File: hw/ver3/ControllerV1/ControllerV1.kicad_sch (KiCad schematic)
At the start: 96 parts, among them J1 SWD Debug, J2 BMS_Serial, J3 Debug, P1 USB_C_Plug_USB2.0, Q1 BSS138, Q2 BSS138, Q3 BSS138, Q4 BSS138, SW1 Boot, SW2 Reset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

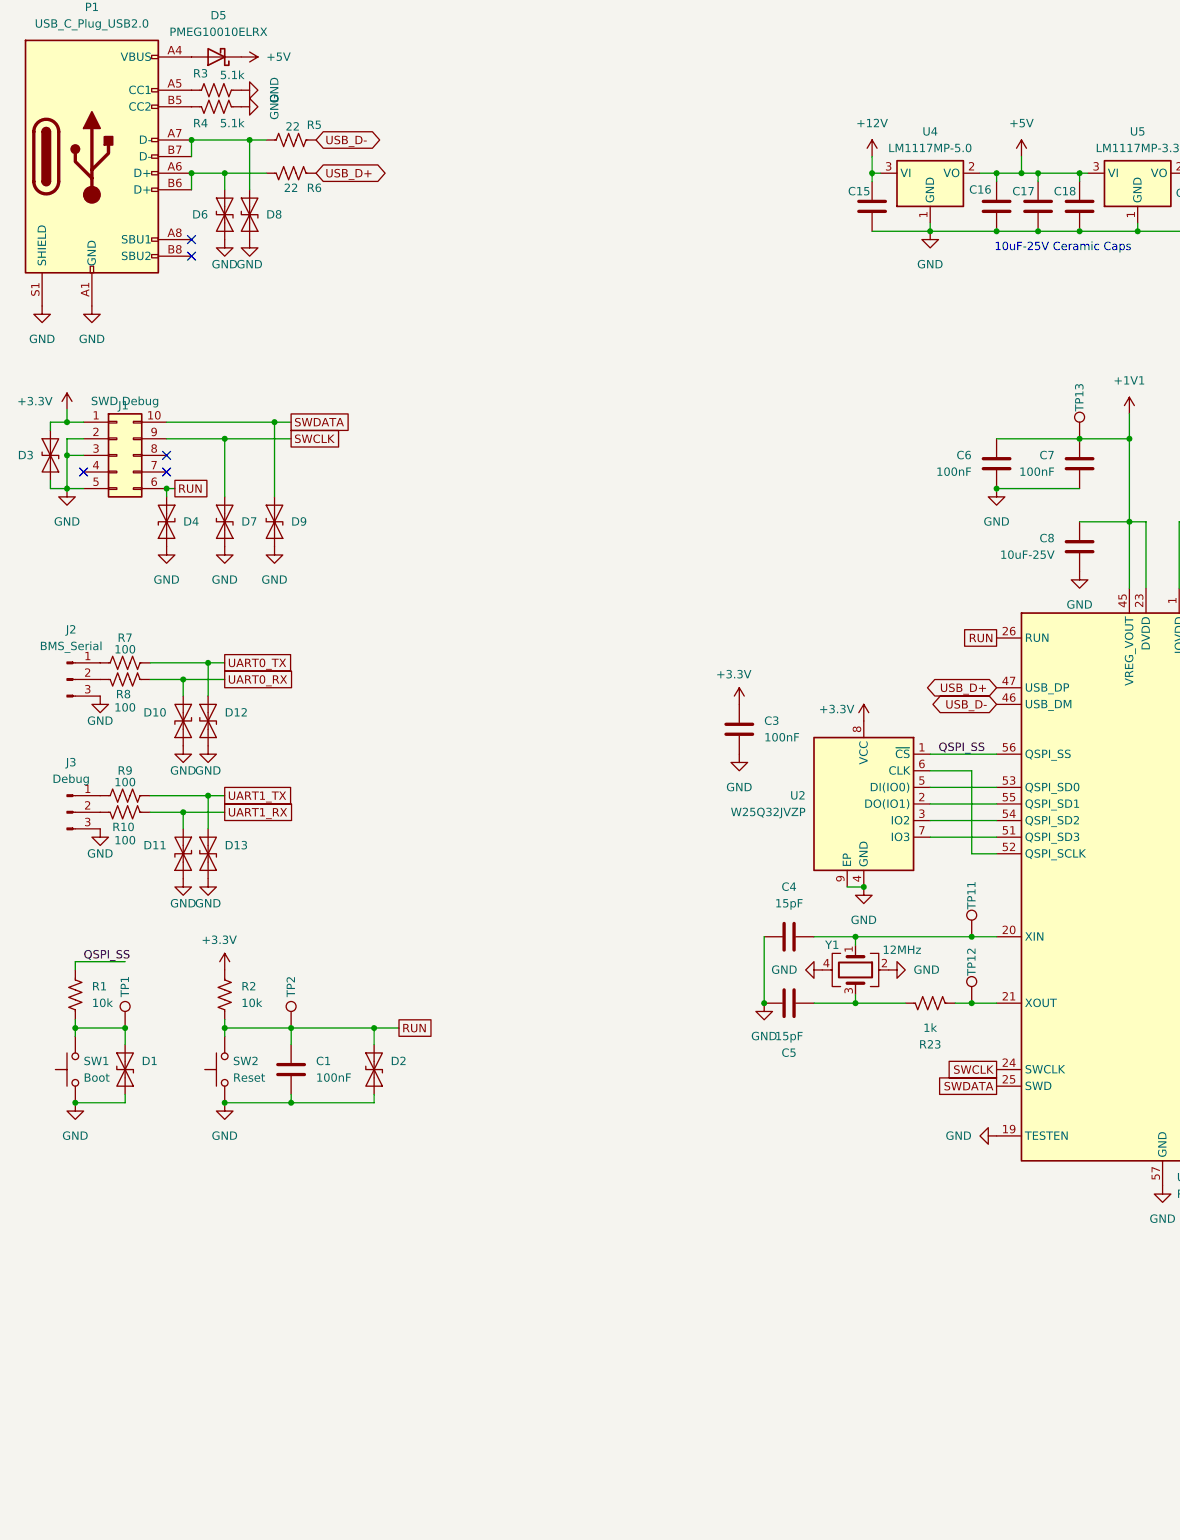
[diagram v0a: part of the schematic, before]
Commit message: Split the design into four major components. Start working on system architecture.
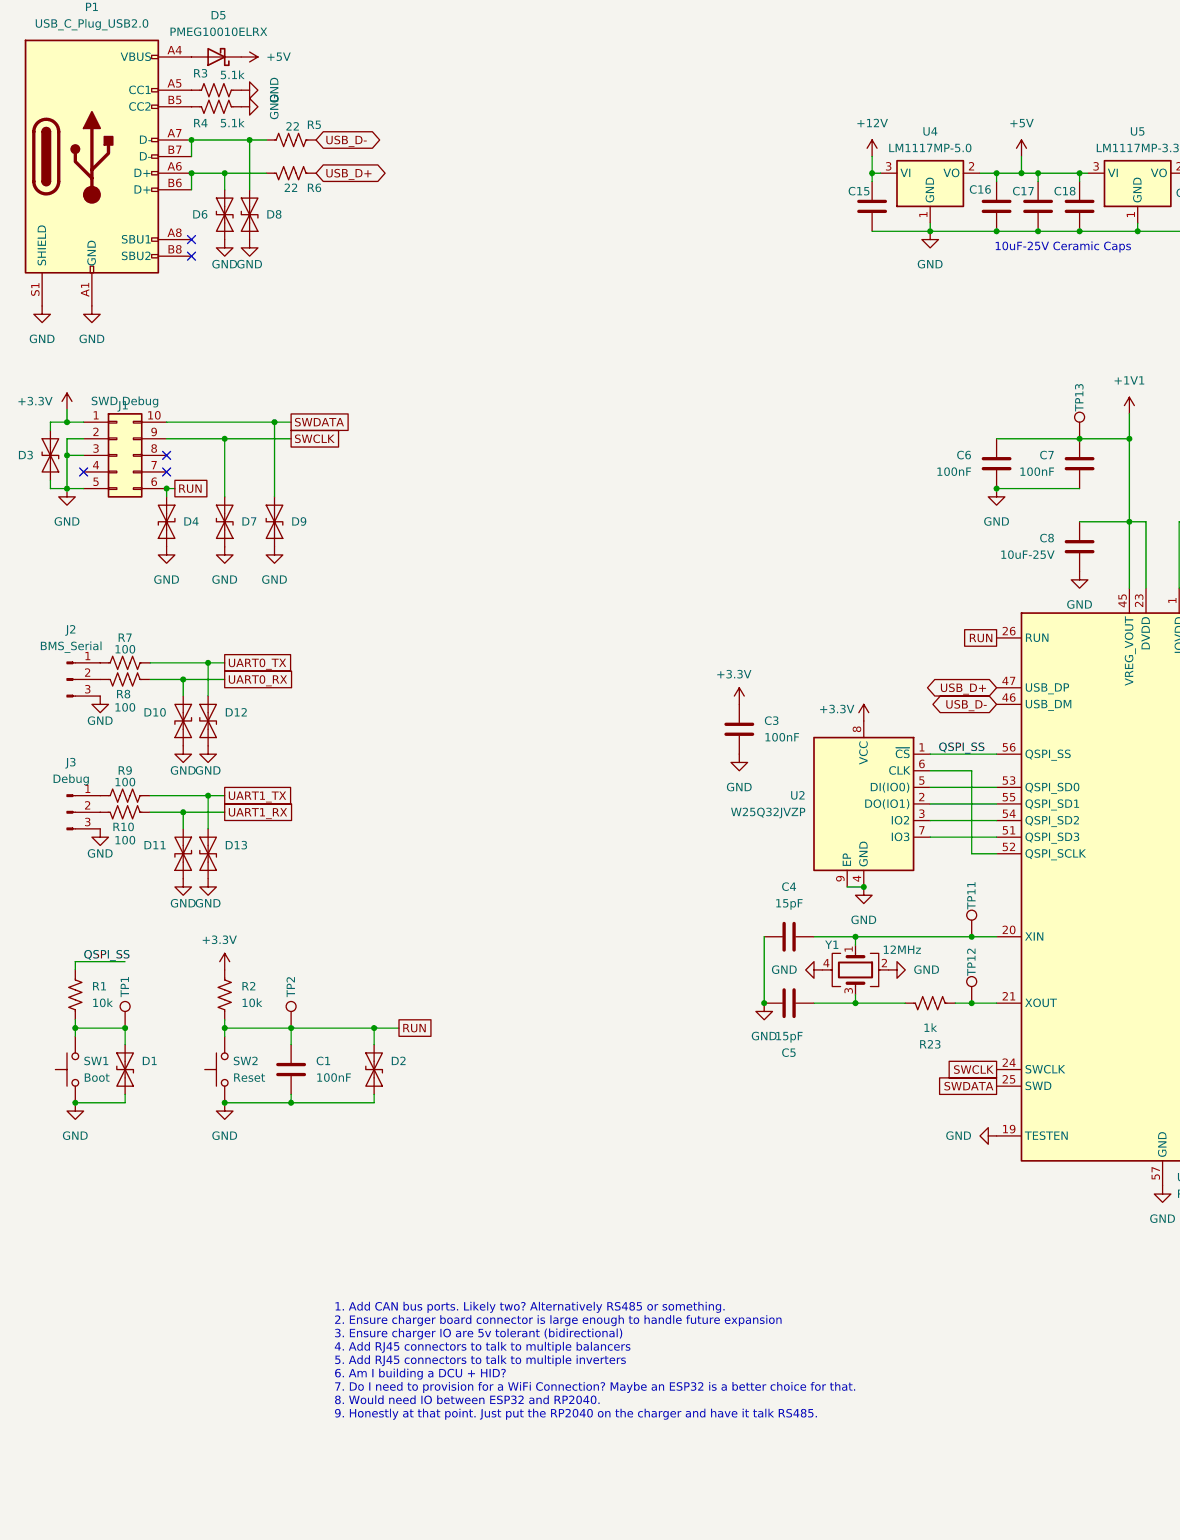
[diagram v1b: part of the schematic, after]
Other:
- note added: "1. Add CAN bus ports. Likely two? Alternatively RS485 or something. 2. Ensure charger board connector is large enough to handle future expansion 3. Ensure charger IO are 5v tolerant (bidirectional) 4. Add RJ45 connectors to talk to multiple balancers 5. Add RJ45 connectors to talk to multiple inverters 6. Am I building a DCU + HID? 7. Do I need to provision for a WiFi Connection? Maybe an ESP32 i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"
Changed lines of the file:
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@@
 (kicad_sch
-	(version 20231120)
+	(version 20250114)
 	(generator "eeschema")
-	(generator_version "8.0")
+	(generator_version "9.0")
 	(paper "A3")
+	(text "10uF-25V Ceramic Caps"
+		(exclude_from_sim no)
+		(at 177.8 53.34 0)
+		(effects
+			(font
+				(size 1.27 1.27)
+			)
+		)
+	)
+	(text "1. Add CAN bus ports. Likely two? Alternatively RS485 or something.\n2. Ensure charger board connector is large enough to handle future expansion\n3. Ensure charger IO are 5v tolerant (bidirectional)\n4. Add RJ45 connectors to talk to multiple balancers\n5. Add RJ45 connectors to talk to multiple inverters\n6. Am I building a DCU + HID?\n7. Do I need to provision for a WiFi Connection? Maybe an ESP32 is a better choice for that.\n8. Would need IO between ESP32 and RP2040.\n9. Honestly at that point. Just put the RP2040 on the charger and have it talk RS485."
+		(exclude_from_sim no)
+		(at 66.294 223.774 0)
+		(effects
+			(font
+				(size 1.27 1.27)
+			)
+			(justify left)
+		)
+	)
 	(junction
 		(at 369.57 54.61)
@@
 		)
 	)
-	(text "10uF-25V Ceramic Caps"
-		(exclude_from_sim no)
-		(at 177.8 53.34 0)
-		(effects
-			(font
-				(size 1.27 1.27)
-			)
-		)
-	)
 	(label "QSPI_SS"
 		(at 27.94 162.56 0)
-		(fields_autoplaced yes)
 		(effects
 			(font
@@
 	(label "SPI1_SCK"
 		(at 219.71 148.59 0)
-		(fields_autoplaced yes)
 		(effects
 			(font
@@
 	(label "SPI1_CSn"
 		(at 361.95 165.1 0)
-		(fields_autoplaced yes)
 		(effects
 			(font
@@
 	(label "SPI1_RX"
 		(at 219.71 143.51 0)
-		(fields_autoplaced yes)
 		(effects
 			(font
@@
 	(label "SPI0_RX"
 		(at 359.41 184.15 0)
-		(fields_autoplaced yes)
 		(effects
 			(font
@@
 	(label "SPI0_RX"
 		(at 219.71 113.03 0)
-		(fields_autoplaced yes)
 		(effects
 			(font
@@
 	(label "QSPI_SS"
 		(at 158.75 130.81 0)
-		(fields_autoplaced yes)
 		(effects
 			(font
@@
 	(label "SPI1_RX"
 		(at 361.95 162.56 0)
-		(fields_autoplaced yes)
 		(effects
 			(font
@@
 	(label "SPI0_SCK"
 		(at 219.71 118.11 0)
-		(fields_autoplaced yes)
 		(effects
 			(font
@@
 	(label "SPI0_CSn"
 		(at 219.71 115.57 0)
-		(fields_autoplaced yes)
 		(effects
 			(font
@@
 	(label "SPI1_TX"
 		(at 219.71 151.13 0)
-		(fields_autoplaced yes)
 		(effects
 			(font
@@
 	(label "SPI0_TX"
 		(at 359.41 181.61 0)
-		(fields_autoplaced yes)
 		(effects
 			(font
@@
 	(label "SPI1_CSn"
 		(at 219.71 146.05 0)
-		(fields_autoplaced yes)
 		(effects
 			(font
@@
 	(label "SPI1_SCK"
 		(at 361.95 167.64 0)
-		(fields_autoplaced yes)
 		(effects
 			(font
@@
 	(label "SPI0_CSn"
 		(at 359.41 176.53 0)
-		(fields_autoplaced yes)
 		(effects
 			(font
@@
 	(label "SPI1_TX"
 		(at 361.95 170.18 0)
-		(fields_autoplaced yes)
 		(effects
 			(font
@@
 	(label "SPI0_TX"
 		(at 219.71 120.65 0)
-		(fields_autoplaced yes)
 		(effects
 			(font
@@
 	(label "SPI0_SCK"
 		(at 359.41 179.07 0)
-		(fields_autoplaced yes)
 		(effects
 			(font
@@
 		(shape output)
 		(at 227.33 151.13 0)
-		(fields_autoplaced yes)
 		(effects
 			(font
@@
 		(shape output)
 		(at 218.44 140.97 0)
-		(fields_autoplaced yes)
 		(effects
 			(font
@@
 		(shape input)
 		(at 218.44 189.23 0)
-		(fields_autoplaced yes)
 		(effects
 			(font
@@
 		(shape output)
 		(at 227.33 148.59 0)
-		(fields_autoplaced yes)
 		(effects
 			(font
@@
 		(shape input)
 		(at 227.33 143.51 0)
-		(fields_autoplaced yes)
 		(effects
 			(font
@@
 		(shape output)
 		(at 227.33 146.05 0)
-		(fields_autoplaced yes)
 		(effects
 			(font
@@
 		)
 	)
+	(embedded_fonts no)
 )

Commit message: Redo some charger routing. Improve design for interconnect
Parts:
- removed C1, C11, C12, C13, C14, C2, C22, C3, C6, C7, C9: 100nF, Capacitor_SMD:C_0603_1608Metric, symbol Device:C
- removed C10, C15, C16, C17, C18, C19, C20, C21, C8: 10uF-25V, Capacitor_SMD:C_0603_1608Metric, symbol Device:C
- removed C4, C5: 15pF, Capacitor_SMD:C_0603_1608Metric, symbol Device:C
- removed D1, D10, D11, D12, D13, D18, D2: ESD9B3.3ST5G, Diode_SMD:D_SOD-923, symbol Diode:ESD9B3.3ST5G
- removed D14, D16: Yellow LED, LED_SMD:LED_0805_2012Metric, symbol Device:LED
- removed D15, D17: Green LED, LED_SMD:LED_0805_2012Metric, symbol Device:LED
- removed D3, D4, D6, D7, D8, D9: ESD9B5.0ST5G, Diode_SMD:D_SOD-923, symbol Diode:ESD9B5.0ST5G
- removed D5: PMEG10010ELRX, Diode_SMD:D_SOD-123, symbol Device:D_Schottky
- removed J1: SWD Debug, Connectors:JTAG_2x05_P1_27mm_Shrouded_SMD, symbol Connector_Generic:Conn_02x05_Counter_Clockwise
- removed J2: BMS_Serial, Connector_PinHeader_2.54mm:PinHeader_1x03_P2.54mm_Vertical, symbol Connector:Conn_01x03_Pin
- removed J3: Debug, Connector_PinHeader_2.54mm:PinHeader_1x03_P2.54mm_Vertical, symbol Connector:Conn_01x03_Pin
- removed P1: USB_C_Plug_USB2.0, Connector_USB:USB_C_Receptacle_GCT_USB4085, symbol Connector:USB_C_Receptacle_USB2.0_16P
- removed Q1, Q2, Q3, Q4: BSS138, Package_TO_SOT_SMD:SOT-23, symbol Transistor_FET:BSS138
- removed R1, R13, R14, R19, R2, R20, R25: 10k, Resistor_SMD:R_0603_1608Metric, symbol Device:R_US
- removed R10, R11, R12, R17, R18, R7, R8, R9: 100, Resistor_SMD:R_0603_1608Metric, symbol Device:R_US
- removed R15, R16, R21, R22: 510, Resistor_SMD:R_0603_1608Metric, symbol Device:R_US
- removed R23: 1k, Resistor_SMD:R_0603_1608Metric, symbol Device:R_US
- removed R24, R26: 100k, Resistor_SMD:R_0603_1608Metric, symbol Device:R_US
- removed R3, R4: 5.1k, Resistor_SMD:R_0603_1608Metric, symbol Device:R_US
- removed R5, R6: 22, Resistor_SMD:R_0603_1608Metric, symbol Device:R_US
- removed SW1: Boot, Button_Switch_SMD:SW_SPST_EVQP2, symbol Switch:SW_Push
- removed SW2: Reset, Button_Switch_SMD:SW_SPST_EVQP2, symbol Switch:SW_Push
- removed TP1, TP10, TP11, TP12, TP13, TP14, TP2, TP3, TP4, TP5, TP6, TP7, TP8, TP9: TestPoint, TestPoint:TestPoint_Pad_D1.0mm, symbol Connector:TestPoint
- removed U1, U2: W25Q32JVZP, Package_SON:WSON-8-1EP_6x5mm_P1.27mm_EP3.4x4.3mm, symbol Memory_Flash:W25Q32JVZP
- removed U3: RP2040, Package_DFN_QFN:QFN-56-1EP_7x7mm_P0.4mm_EP3.2x3.2mm, symbol MCU_RaspberryPi:RP2040
- removed U4: LM1117MP-5.0, Package_TO_SOT_SMD:SOT-223-3_TabPin2, symbol Regulator_Linear:LM1117MP-5.0
- removed U5: LM1117MP-3.3, Package_TO_SOT_SMD:SOT-223-3_TabPin2, symbol Regulator_Linear:LM1117MP-3.3
- removed Y1: 12MHz, Crystal:Crystal_SMD_3225-4Pin_3.2x2.5mm, symbol Device:Crystal_GND24
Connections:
- no-connect marks 5 -> 0
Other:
- note removed: "1. Add CAN bus ports. Likely two? Alternatively RS485 or something. 2. Ensure charger board connector is large enough to handle future expansion 3. Ensure charger IO are 5v tolerant (bidirectional) 4. Add RJ45 connectors to talk to multiple balancers 5. Add RJ45 connectors to talk to multiple inverters 6. Am I building a DCU + HID? 7. Do I need to provision for a WiFi Connection? Maybe an ESP32 i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"
- note removed: "10uF-25V Ceramic Caps"
